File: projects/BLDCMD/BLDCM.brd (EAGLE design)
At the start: 80 x 50 mm, 74 parts, among them IC1 STM32F103C8, IC10 7805DT, IC3 NCV7351D1E, IC4 74AHCT1G08DCK, IC5 74AHCT1G08DCK, IC6 74AHCT1G08DCK, IC7 SI8621AB-B-IS, IC8 7815DT, IC9 MC34063AD, Q1 N-MOSFET-, Q2 N-MOSFET-, Q3 N-MOSFET-, Q4 N-MOSFET-, Q5 N-MOSFET-, Q6 N-MOSFET-, X1 8P8C-LED

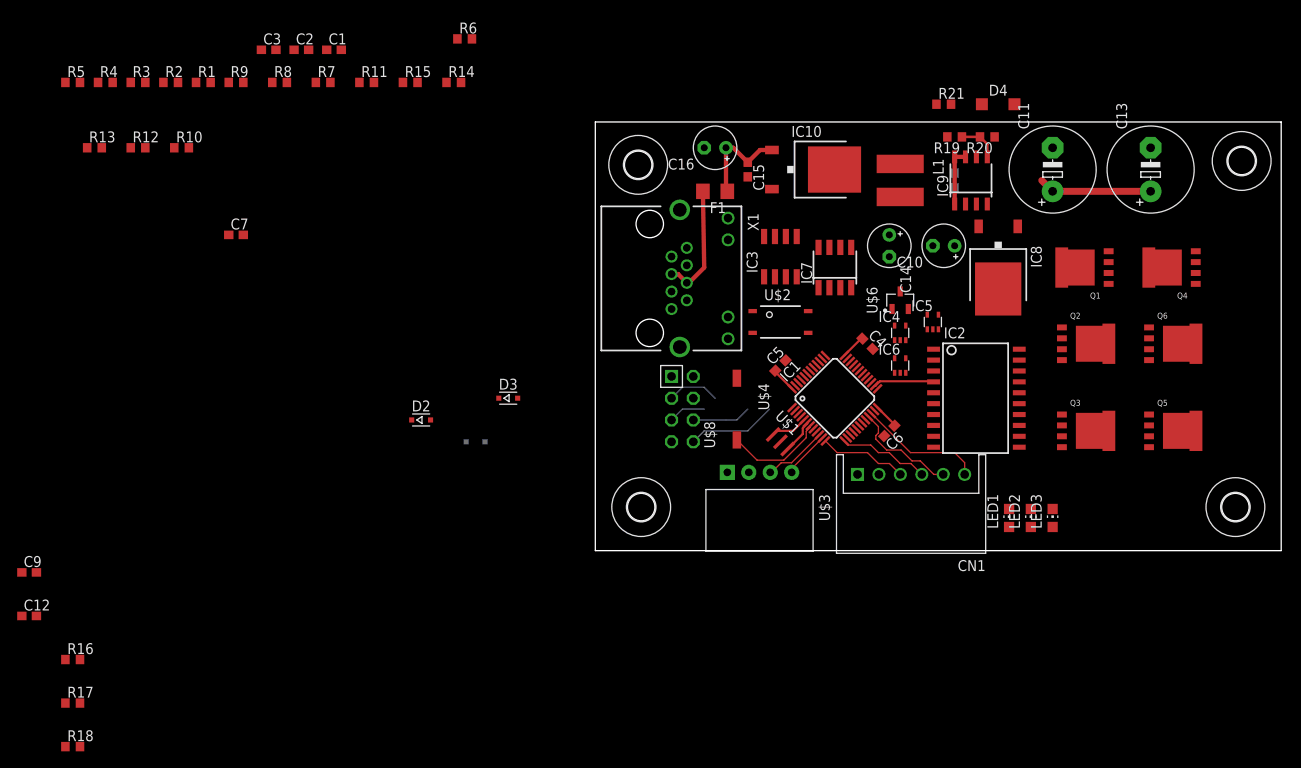
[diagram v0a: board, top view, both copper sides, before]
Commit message: usbcan 修正済み　BLDCMD完成
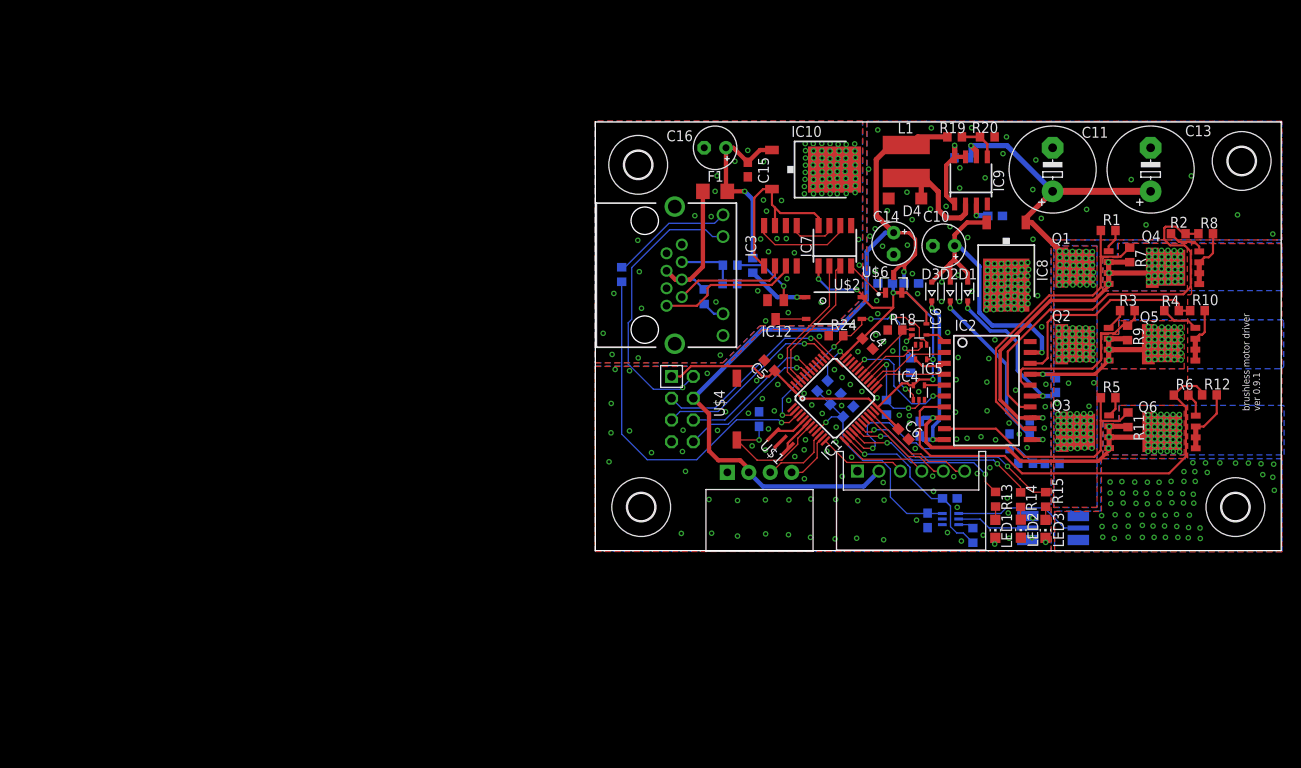
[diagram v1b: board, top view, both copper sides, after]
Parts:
- added B1: FERRITE_BEAD, mylib:R0603
- added C17, C18, C19: (no value), rcl:C0603
- added C20: 10u, rcl:C0603
- added C21: 1u, rcl:C0603
- added IC12: BSS138BK, mylib:SOT23
- added R22, R24: 1k, mylib:R0603
- added R23: 100k, mylib:R0603
- added R25: 1k?, mylib:R0603
- added R26: 4k7, mylib:R0603
- added R27: 470, mylib:R0603
- added R28: CSS2H-2512, mylib:CSS2H-2512
- added R29, R30, R31: 10, mylib:R0603
- added U$5: NCS199, mylib:SOT65P210X110-6
- X1: device con-rj45:8P8C-LED -> mylib:8P8C-LED
- moved R12 128.3 mm to (71.6, 18.2)
- moved R4 127.2 mm to (67.2, 28.0), turned to 180 degrees
- moved R5 126.3 mm to (59.8, 17.8)
- moved R10 120.0 mm to (70.2, 28.0)
- moved R2 118.8 mm to (68.0, 37.0), turned to 180 degrees
- moved R3 118.4 mm to (62.1, 28.0), turned to 180 degrees
- moved R13 112.8 mm to (46.7, 5.99), turned to 270 degrees
- moved R8 109.5 mm to (71.2, 37.0)
- moved C9 108.3 mm to (36.9, 31.2), flipped to the bottom, turned to 180 degrees
- moved R9 108.0 mm to (62.1, 25.4), turned to 270 degrees
- moved R18 107.5 mm to (35.0, 25.7)
- moved C12 107.1 mm to (33.8, 31.2), flipped to the bottom
- moved R1 106.9 mm to (59.8, 37.3)
- moved R17 105.4 mm to (36.8, 21.6), flipped to the bottom, turned to 90 degrees
- moved R16 99.4 mm to (34.0, 16.7), flipped to the bottom, turned to 90 degrees
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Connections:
- removed net AGND: C4.2, C5.2, C6.2, C7.2, CN1.1, IC1.23, IC1.35, IC1.44, IC1.47, IC2.20, LED1.C, LED2.C, LED3.C, R16.1, R17.1, R18.1, U$1.2, U$3.P$1, U$4.P$1, U$8.2, U$8.7, X1.YC
- removed net GND: IC4.3, IC5.3, IC6.3
- new net 3V3A: B1.1, C18.1, C20.1, C21.1, IC1.9, U$5.3
- new net N$31: IC12.1, R22.1
- new net N$32: IC12.3, U$2.2
- new net N$33: R25.1, U$2.1
- new net N$36: R26.1, X1.GA
- new net N$37: R29.1, U$5.6
- new net N$38: R27.1, X1.YA
- net !EMS: now also R24.2, U$2.3; no longer U$2.2
- net +3V3: now also B1.2, IC4.5, IC5.5, IC6.5, U$2.4; no longer U$2.1
- net 24V_ISO: now also R25.2
- net GNDA: now also C17.2, C18.2, C19.2, C20.2, C21.2, C4.2, C5.2, C6.2, C7.2, CN1.1, IC1.23, IC1.35, IC1.44, IC1.47, IC1.8, IC2.20, IC4.3, IC5.3, IC6.3, LED1.C, LED2.C, LED3.C, R16.1, R17.1, R18.1, R24.1, R28.1$1, R28.1$2, R31.1, U$1.2, U$3.P$1, U$4.P$1, U$5.1, U$5.2, U$8.2, U$8.7, X1.YC
- net GNDIO: now also IC12.2, R23.1, X1.GC
- net ISENSE: now also C17.1, R29.2
- net LED_CAN: now also R27.2; no longer X1.YA
- net N$18: now also Q5.1, Q5.2, Q5.3, Q6.1, Q6.2, Q6.3, R10.2, R12.2, R28.2$1, R28.2$2
- net N$19: now also R28.2S, U$5.4; no longer Q5.1, Q5.2, Q5.3, R10.2
- net N$20: now also R28.1S, U$5.5; no longer Q6.1, Q6.2, Q6.3, R12.2
- net N$22: now also R22.2, R23.2
- net N$26: now also R26.2
- net VCC: now also R30.2; no longer IC4.5, IC5.5, IC6.5
- net VSENSE: now also C19.1, R30.1, R31.2
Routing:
- net +5V: track 0.00 -> 93.4 mm, vias 0 -> 1
- net +3V3: track 8.78 -> 86.1 mm, vias 0 -> 6
- net LO3: track 0.00 -> 52.4 mm
- net LO1: track 0.00 -> 46.2 mm
- net LED_CAN: track 0.00 -> 42.1 mm, vias 0 -> 1
- net U: track 0.00 -> 42.0 mm, vias 0 -> 40
- net W: track 0.00 -> 40.7 mm, vias 0 -> 46
- net GNDA: track 0.00 -> 40.0 mm, vias 0 -> 206
- net !EMS: track 0.00 -> 38.0 mm, vias 0 -> 5
- net +15V: track 0.00 -> 37.3 mm, vias 0 -> 1
- net HO1: track 0.00 -> 37.1 mm
- net HO3: track 0.00 -> 29.6 mm
- net VSENSE: track 0.00 -> 29.2 mm, vias 0 -> 1
- net 3V3A: track 0.00 -> 27.9 mm, vias 0 -> 1
- net VCC: track 13.2 -> 39.3 mm, vias 0 -> 113
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- added copper zone on layer 1, net GNDA
- added copper zone on layer 16, net GNDA
- added copper zone on layer 1, net GNDIO
- added copper zone on layer 16, net GNDIO
- added copper zone on layer 1, net N$18
- added copper zone on layer 16, net N$18
- added copper zone on layer 1, net U
- added copper zone on layer 16, net U
- added copper zone on layer 1, net V
- added copper zone on layer 16, net V
- added copper zone on layer 1, net VCC
- added copper zone on layer 16, net VCC
- added copper zone on layer 1, net W
- added copper zone on layer 16, net W
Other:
- board text added: "brushless motor driver ver 0.9.1"
